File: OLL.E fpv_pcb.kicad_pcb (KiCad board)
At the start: 6 copper layers, 47.6 x 41.5 mm, 131 parts, among them J1 Micro_SD_Card, J10 Conn_01x05_Pin, J2 RC, J8 reciver, J9 TYPE-C-31-M-12, M1 M1 front left, M2 m4 rear left, M3 M2 front right, M4 M3 rear right, Q1 2N7002, SW1 SW_SPST, SW2 SW_SPST, U1 MP2315GJ, U10 AON7410, U11 UCC27511ADBV, U12 AON7410, U13 BMP280, U14 STM32H753VITx, U15 USBLC6-2SC6, U3 MP2315GJ, U4 ICM-42688-P, U5 UCC27511ADBV, U6 ul_AON7410, U7 UCC27511ADBV, U8 AON7410, U9 UCC27511ADBV, Y2 8HMz

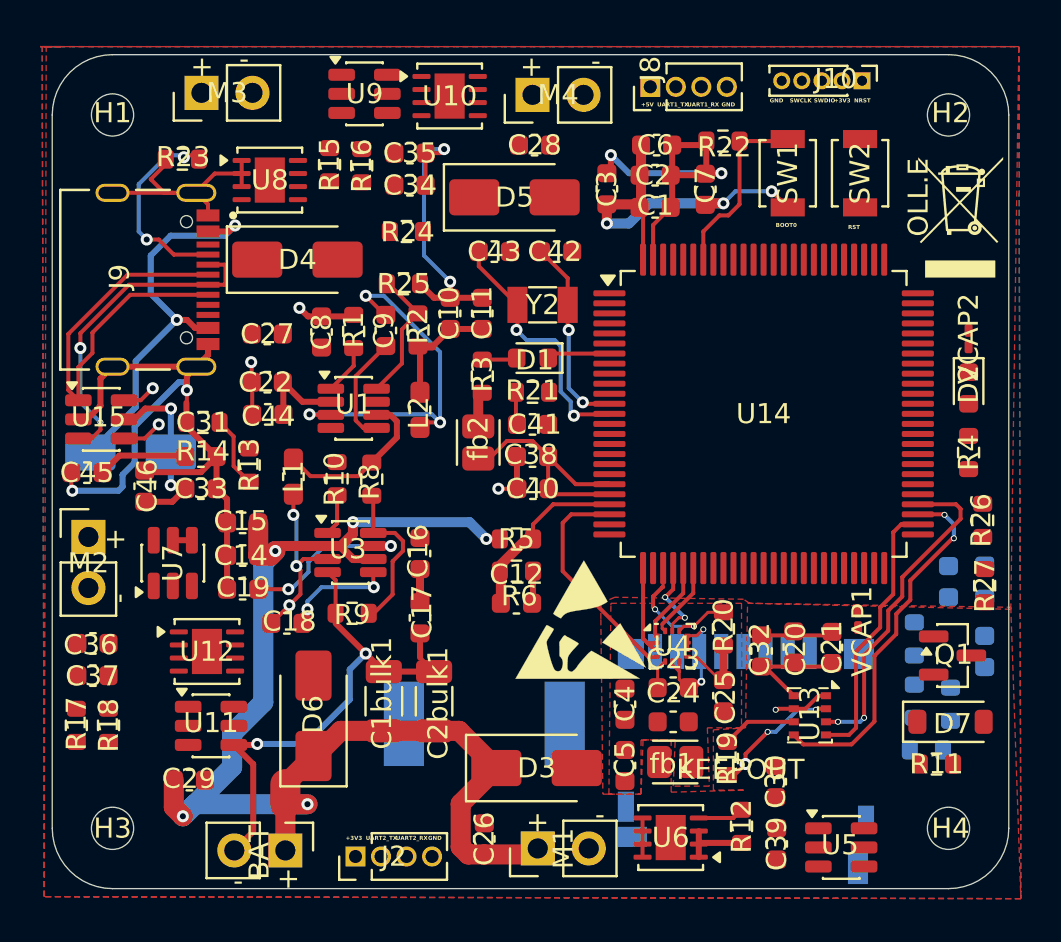
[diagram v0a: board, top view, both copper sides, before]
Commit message: update UART track 0.2mm
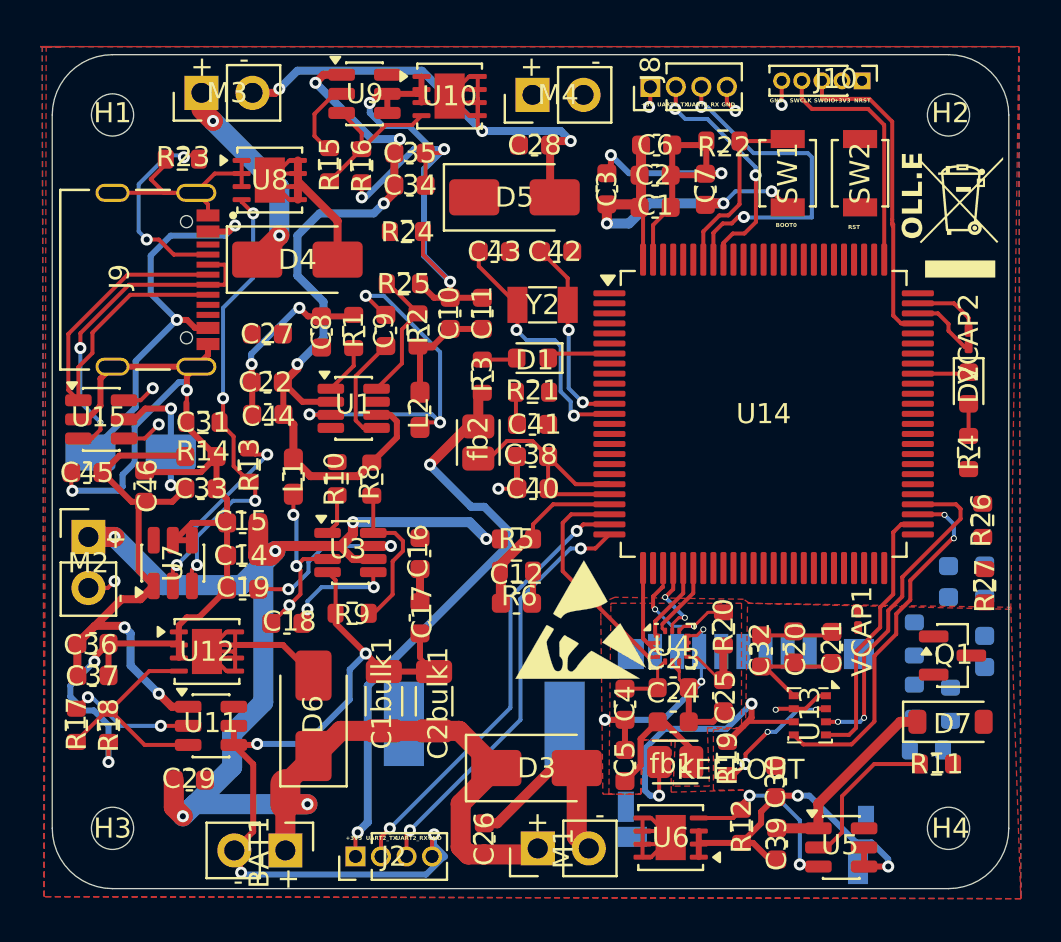
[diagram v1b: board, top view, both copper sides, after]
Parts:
- removed the REF** at (250.9, 42.9)
- M2: value m4 rear left -> M2 front right
- M3: value M2 front right -> M3 rear right
- M4: value M3 rear right -> m4 rear left
- renumbered BAT to BAT1
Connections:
- D3 pad 1: +VBAT -> (no net)
- D3 pad 2: GND -> Net-(C26--)
- D4 pad 1: (no net) -> +VBAT
- D4 pad 2: (no net) -> Net-(C27--)
- D5 pad 1: (no net) -> +VBAT
- D5 pad 2: (no net) -> Net-(C28--)
- D6 pad 2: (no net) -> Net-(C29--)
- M1 pad 2: GND -> Net-(C26--)
- M2 pad 2: Net-(C29--) -> Net-(C27--)
- M3 pad 2: GND -> Net-(C28--)
- M4 pad 2: Net-(C28--) -> Net-(C29--)
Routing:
- net GND: track 141.0 -> 232.9 mm, vias 14 -> 25
- net +5V_FC: track 28.3 -> 88.0 mm, vias 2 -> 9
- net +3V3_FC: track 36.5 -> 77.6 mm, vias 3 -> 7
- net Net-(C28--): track 0.00 -> 31.9 mm, vias 0 -> 3
- net UART2_TX: track 0.00 -> 22.0 mm, vias 0 -> 2
- net +VBAT: track 66.3 -> 87.7 mm, vias 5 -> 8
- net UART2_RX: track 0.00 -> 20.9 mm, vias 0 -> 2
- net Net-(R13-+): track 3.56 -> 22.8 mm, vias 0 -> 4
- net UART1_RX: track 0.00 -> 17.1 mm, vias 0 -> 2
- net Net-(C26--): track 1.95 -> 18.6 mm
- net SWDIO: track 0.00 -> 16.0 mm
- net Net-(C27--): track 0.00 -> 14.8 mm, vias 0 -> 1
- net Net-(C29--): track 0.00 -> 14.6 mm
- net SWCLK: track 0.00 -> 12.2 mm
- net UART1_TX: track 0.00 -> 11.9 mm, vias 0 -> 2
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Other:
- board text added: "OLL.E"

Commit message: fix all error
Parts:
- moved C47 82.2 mm to (179.7, 101.8), turned to 90 degrees
- moved C16 82.1 mm to (151.7, 97.0)
- moved D4 82.1 mm to (145.6, 82.4)
- moved R2 82.1 mm to (151.6, 85.9)
- moved R23 82.1 mm to (139.9, 77.4)
- moved R6 82.1 mm to (156.5, 97.9)
- moved U9 82.1 mm to (148.9, 74.2)
- moved BAT1 82.1 mm to (145.0, 111.8)
- moved C10 82.1 mm to (153.2, 85.1)
- moved C12 82.1 mm to (156.5, 99.5)
- moved C14 82.1 mm to (142.9, 97.1)
- moved C15 82.1 mm to (142.9, 95.5)
- moved C17 82.1 mm to (151.7, 100.2)
- moved C18 82.1 mm to (145.1, 100.5)
- moved C19 82.1 mm to (142.9, 98.8)
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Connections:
- C41 pad 1: Net-(C41-+) -> NRST
- D3 pad 1: (no net) -> +VBAT
- D7 pad 1: +5V_FC -> Net-(D7-K)
- D7 pad 2: Net-(D7-A) -> +5V_FC
- LS1 pad 1: (no net) -> Net-(D7-K)
- LS1 pad 2: (no net) -> +5V_FC
- Q1 pad 3: Net-(D7-A) -> Net-(D7-K)
- R21 pad 1: Net-(C41-+) -> NRST
- SW2 pad 1: Net-(C41-+) -> NRST
- U14 pad 14: Net-(C41-+) -> NRST
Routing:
- net CMD: track 0.00 -> 117.5 mm, vias 0 -> 3
- net GND: track 232.9 -> 330.6 mm, vias 25 -> 33
- net +5V_FC: track 88.0 -> 180.4 mm, vias 9 -> 15
- net +3V3_FC: track 77.6 -> 165.0 mm, vias 7 -> 14
- net +VBAT: track 87.7 -> 172.5 mm, vias 8 -> 9
- net C1_D0: track 0.00 -> 66.3 mm, vias 0 -> 6
- net C1_D1: track 0.00 -> 49.1 mm, vias 0 -> 2
- net Net-(C29--): track 14.6 -> 56.1 mm, vias 0 -> 3
- net MOTOR3: track 0.00 -> 40.6 mm, vias 0 -> 2
- net USB D+: track 1.67 -> 41.2 mm, vias 1 -> 2
- net USB D−: track 2.01 -> 41.5 mm, vias 1 -> 2
- net MOTOR2: track 0.00 -> 36.6 mm, vias 0 -> 2
- net C1_D3: track 0.00 -> 35.3 mm, vias 0 -> 3
- net C1_D2: track 0.00 -> 34.5 mm, vias 0 -> 3
- net NRST: track 0.00 -> 34.2 mm, vias 0 -> 4
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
